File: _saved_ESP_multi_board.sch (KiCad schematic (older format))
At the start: 25 parts, among them P101 CONN_01X02, P102 CONN_01X06, P103 CONN_01X02, P104 CONN_01X06, P105 CONN_01X12, P106 CONN_01X03, P108 CONN_I2C_MPU6050, U101 L293DD, U102 ESP-12, U103 MAX11605EEE+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

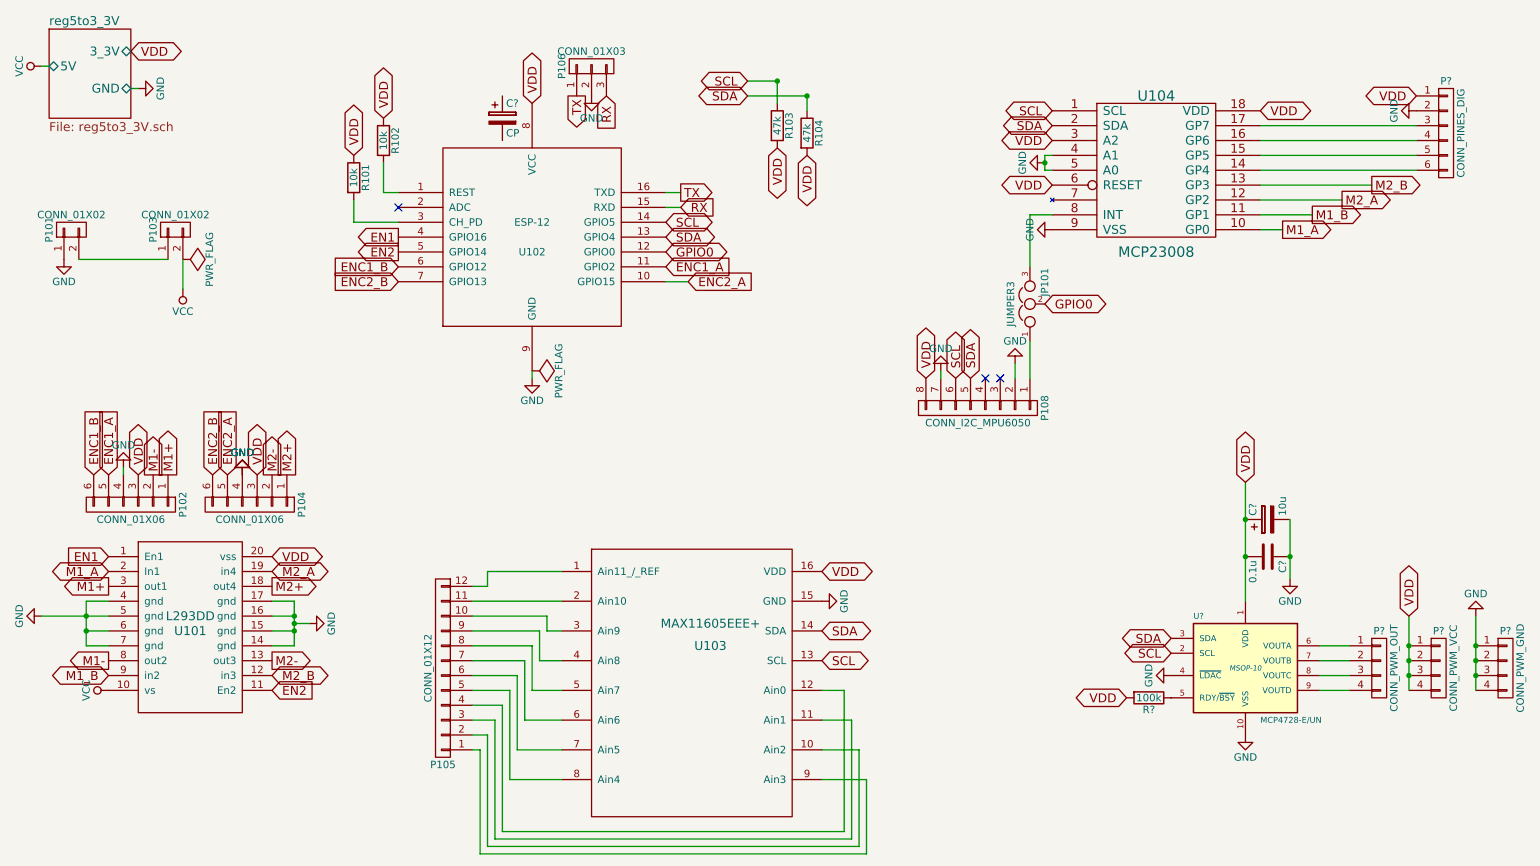
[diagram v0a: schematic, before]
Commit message: modificada huella del jumper, incluidos condensadores en la linea de 3.3v
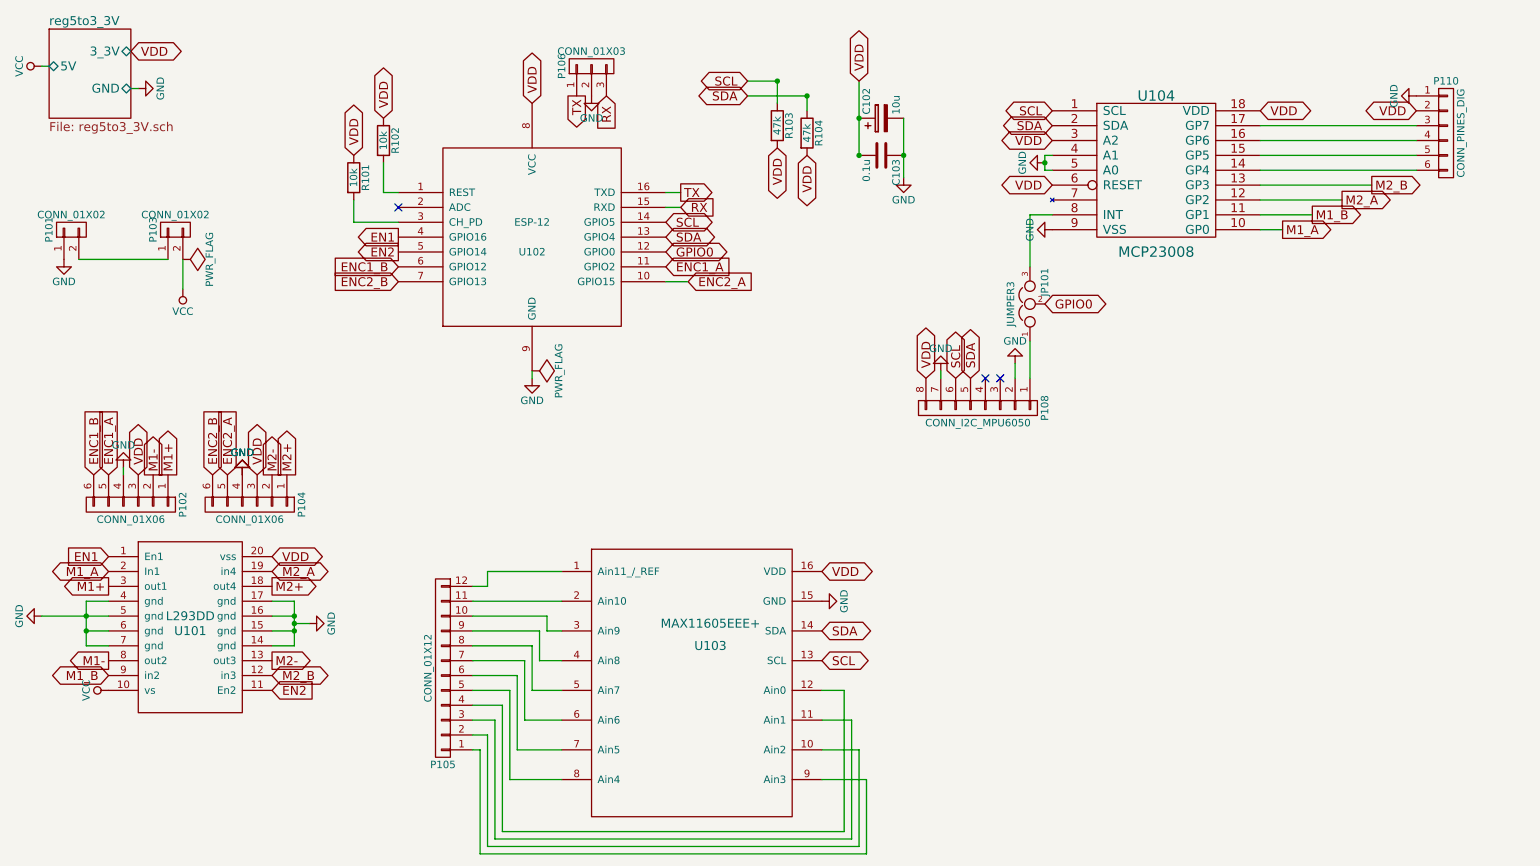
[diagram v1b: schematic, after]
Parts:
- removed C?: CP, symbol CP
- removed P?: CONN_PWM_OUT, symbol CONN_01X04
- removed P?: CONN_PWM_VCC, symbol CONN_01X04
- removed P?: CONN_PWM_GND, symbol CONN_01X04
- removed R?: 100k, symbol R
- removed U?: MCP4728-E/UN, MSOP-10, symbol MCP4728-E/UN
- C102: renamed from C?; footprint (none) -> Capacitors_Tantalum_SMD:TantalC_SizeC_EIA-6032_HandSoldering
- C103: renamed from C?; footprint (none) -> Capacitors_SMD:C_0805_HandSoldering
- P110: renamed from P?; footprint (none) -> Pin_Headers:Pin_Header_Straight_1x06
- R101, R102, R103, R104: footprint Resistors_SMD:R_1812_HandSoldering -> Resistors_SMD:R_0805_HandSoldering
- U103: footprint Housings_SSOP:QSOP-16_3.9x4.9mm_Pitch0.635mm -> Housings_SSOP:SSOP-16_5.3x6.2mm_Pitch0.65mm
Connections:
- net GND: now also P110.1 (P1); no longer P110.2 (P2)
- net VDD: now also P110.2 (P2); no longer P110.1 (P1)
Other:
- moved on the sheet: C102, C103
